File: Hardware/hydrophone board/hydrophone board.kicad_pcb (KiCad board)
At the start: 4 copper layers, 147.3 x 66 mm, 164 parts, among them J1 AudioJack3_Ground, J111 Conn_01x02, J121 Conn_01x02, J131 Conn_01x02, J141 Conn_01x02, J2 AudioJack3_Ground, J211 Conn_01x02, J221 Conn_01x02, J231 Conn_01x02, J241 Conn_01x02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

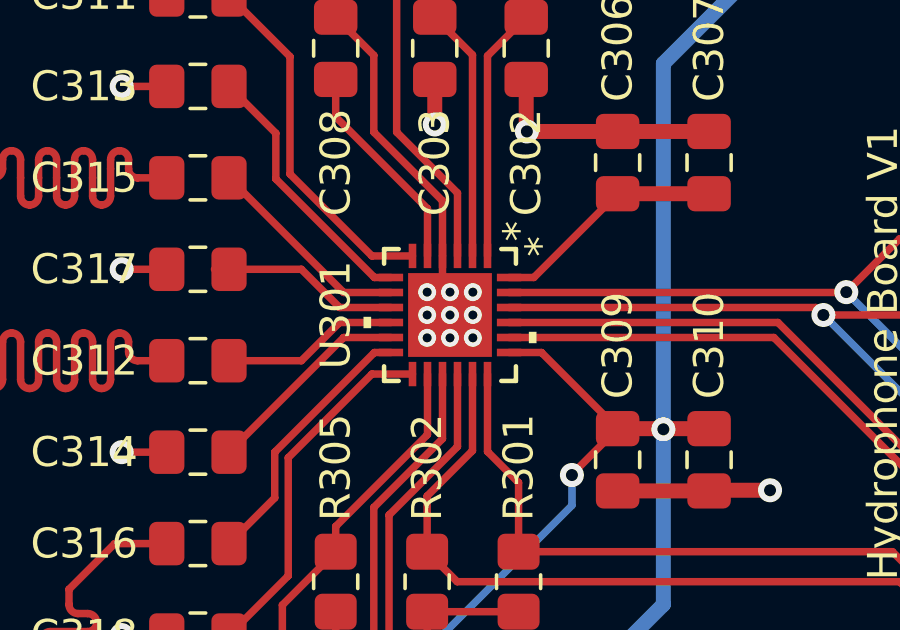
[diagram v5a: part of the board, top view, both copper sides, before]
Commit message: changed iovdd cap, thermal pad via size
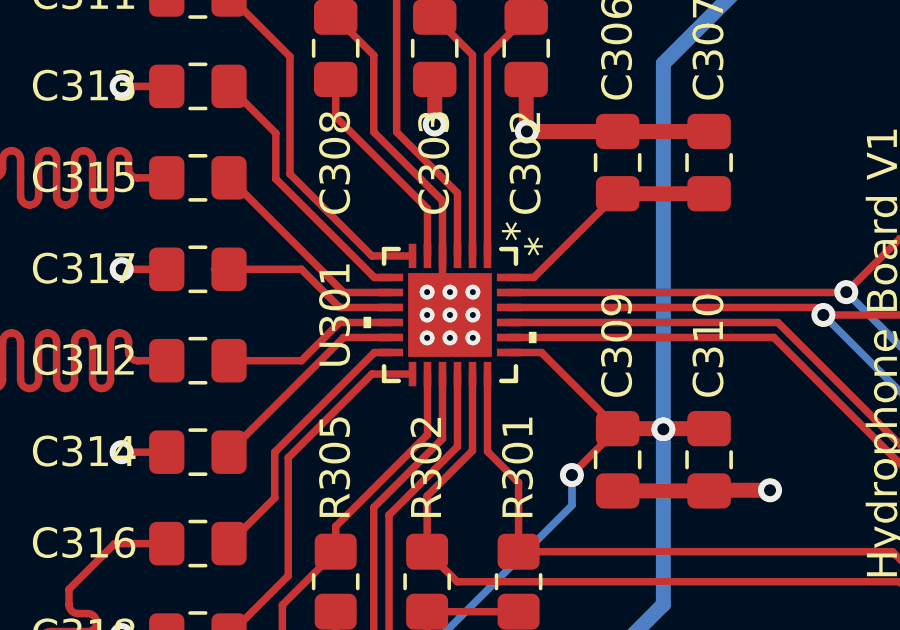
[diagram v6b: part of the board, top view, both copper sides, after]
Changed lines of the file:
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@@
   (segment (start 156.929 67.056) (end 155.4265 67.056) (width 0.25) (layer "F.Cu") (net 1))
   (via (at 146.05 77.724) (size 0.8) (drill 0.4) (layers "F.Cu" "B.Cu") (net 1))
-  (via (at 167.132 69.342) (size 0.6) (drill 0.3) (layers "F.Cu" "B.Cu") (net 1))
+  (via (at 167.132 69.342) (size 0.5) (drill 0.2) (layers "F.Cu" "B.Cu") (net 1))
   (via (at 177.038 87.884) (size 0.8) (drill 0.4) (layers "F.Cu" "B.Cu") (net 1))
   (via (at 135.128 45.72) (size 0.8) (drill 0.4) (layers "F.Cu" "B.Cu") (net 1))
   (via (at 172.974 95.25) (size 0.8) (drill 0.4) (layers "F.Cu" "B.Cu") (net 1))
-  (via (at 166.37 69.342) (size 0.6) (drill 0.3) (layers "F.Cu" "B.Cu") (net 1))
+  (via (at 166.37 69.342) (size 0.5) (drill 0.2) (layers "F.Cu" "B.Cu") (net 1))
   (via (at 98.044 81.28) (size 0.8) (drill 0.4) (layers "F.Cu" "B.Cu") (net 1))
   (via (at 101.6 73.66) (size 0.8) (drill 0.4) (layers "F.Cu" "B.Cu") (net 1))
@@
   (via (at 101.6 58.42) (size 0.8) (drill 0.4) (layers "F.Cu" "B.Cu") (net 1))
   (via (at 105.156 96.52) (size 0.8) (drill 0.4) (layers "F.Cu" "B.Cu") (net 1))
-  (via (at 167.132 68.58) (size 0.6) (drill 0.3) (layers "F.Cu" "B.Cu") (net 1))
+  (via (at 167.132 68.58) (size 0.5) (drill 0.2) (layers "F.Cu" "B.Cu") (net 1))
   (via (at 168.9315 62.4625) (size 0.8) (drill 0.4) (layers "F.Cu" "B.Cu") (net 1))
   (via (at 146.05 62.484) (size 0.8) (drill 0.4) (layers "F.Cu" "B.Cu") (net 1))
@@
   (via (at 71.374 97.563) (size 0.8) (drill 0.4) (layers "F.Cu" "B.Cu") (net 1))
   (via (at 165.1 97.282) (size 0.8) (drill 0.4) (layers "F.Cu" "B.Cu") (net 1))
-  (via (at 165.608 69.342) (size 0.6) (drill 0.3) (layers "F.Cu" "B.Cu") (net 1))
+  (via (at 165.608 69.342) (size 0.5) (drill 0.2) (layers "F.Cu" "B.Cu") (net 1))
   (via (at 120.904 86.3815) (size 0.8) (drill 0.4) (layers "F.Cu" "B.Cu") (net 1))
   (via (at 101.6 43.18) (size 0.8) (drill 0.4) (layers "F.Cu" "B.Cu") (net 1))
@@
   (via (at 117.348 76.2) (size 0.8) (drill 0.4) (layers "F.Cu" "B.Cu") (net 1))
   (via (at 164.084 83.804) (size 0.8) (drill 0.4) (layers "F.Cu" "B.Cu") (net 1))
-  (via (at 166.37 67.818) (size 0.6) (drill 0.3) (layers "F.Cu" "B.Cu") (net 1))
-  (via (at 167.132 67.818) (size 0.6) (drill 0.3) (layers "F.Cu" "B.Cu") (net 1))
+  (via (at 166.37 67.818) (size 0.5) (drill 0.2) (layers "F.Cu" "B.Cu") (net 1))
+  (via (at 167.132 67.818) (size 0.5) (drill 0.2) (layers "F.Cu" "B.Cu") (net 1))
   (via (at 177.038 74.422) (size 0.8) (drill 0.4) (layers "F.Cu" "B.Cu") (net 1))
-  (via (at 165.608 67.818) (size 0.6) (drill 0.3) (layers "F.Cu" "B.Cu") (net 1))
+  (via (at 165.608 67.818) (size 0.5) (drill 0.2) (layers "F.Cu" "B.Cu") (net 1))
   (via (at 175.768 97.282) (size 0.8) (drill 0.4) (layers "F.Cu" "B.Cu") (net 1))
   (via (at 172.974 93.98) (size 0.8) (drill 0.4) (layers "F.Cu" "B.Cu") (net 1))
@@
   (via (at 98.044 50.8) (size 0.8) (drill 0.4) (layers "F.Cu" "B.Cu") (net 1))
   (via (at 168.656 97.282) (size 0.8) (drill 0.4) (layers "F.Cu" "B.Cu") (net 1))
-  (via (at 165.608 68.58) (size 0.6) (drill 0.3) (layers "F.Cu" "B.Cu") (net 1))
+  (via (at 165.608 68.58) (size 0.5) (drill 0.2) (layers "F.Cu" "B.Cu") (net 1))
   (via (at 155.4265 79.248) (size 0.8) (drill 0.4) (layers "F.Cu" "B.Cu") (net 1))
   (via (at 105.156 50.8) (size 0.8) (drill 0.4) (layers "F.Cu" "B.Cu") (net 1))
   (via (at 146.05 47.244) (size 0.8) (drill 0.4) (layers "F.Cu" "B.Cu") (net 1))
   (via (at 105.156 81.2585) (size 0.8) (drill 0.4) (layers "F.Cu" "B.Cu") (net 1))
-  (via (at 166.37 68.58) (size 0.6) (drill 0.3) (layers "F.Cu" "B.Cu") (net 1))
+  (via (at 166.37 68.58) (size 0.5) (drill 0.2) (layers "F.Cu" "B.Cu") (net 1))
   (via (at 160.782 55.626) (size 0.8) (drill 0.4) (layers "F.Cu" "B.Cu") (net 1))
   (via (at 170.18 97.282) (size 0.8) (drill 0.4) (layers "F.Cu" "B.Cu") (net 1))

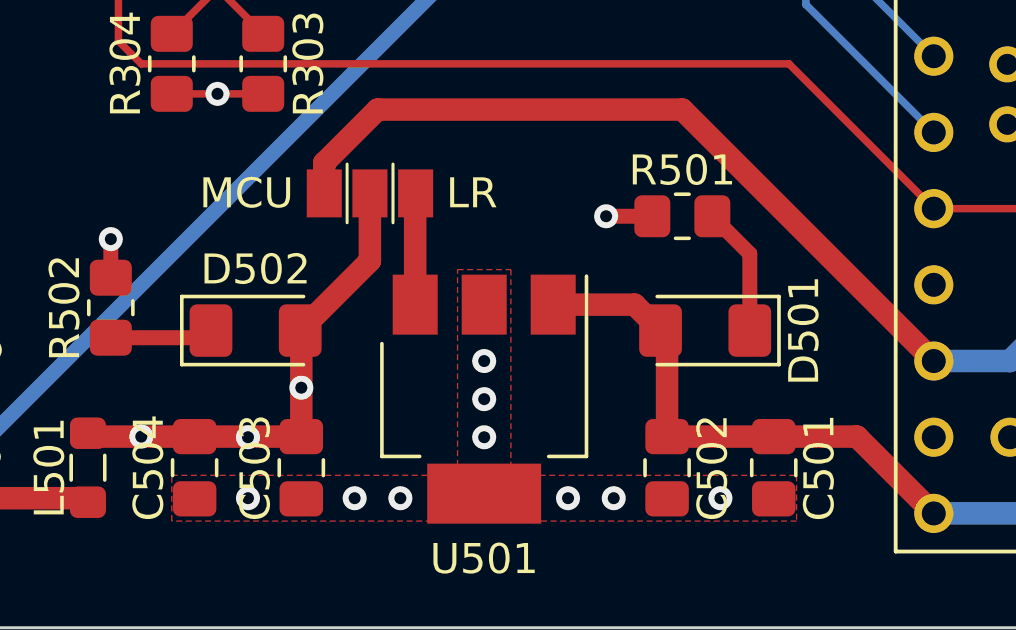
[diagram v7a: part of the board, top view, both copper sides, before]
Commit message: changed led footprint to 0805
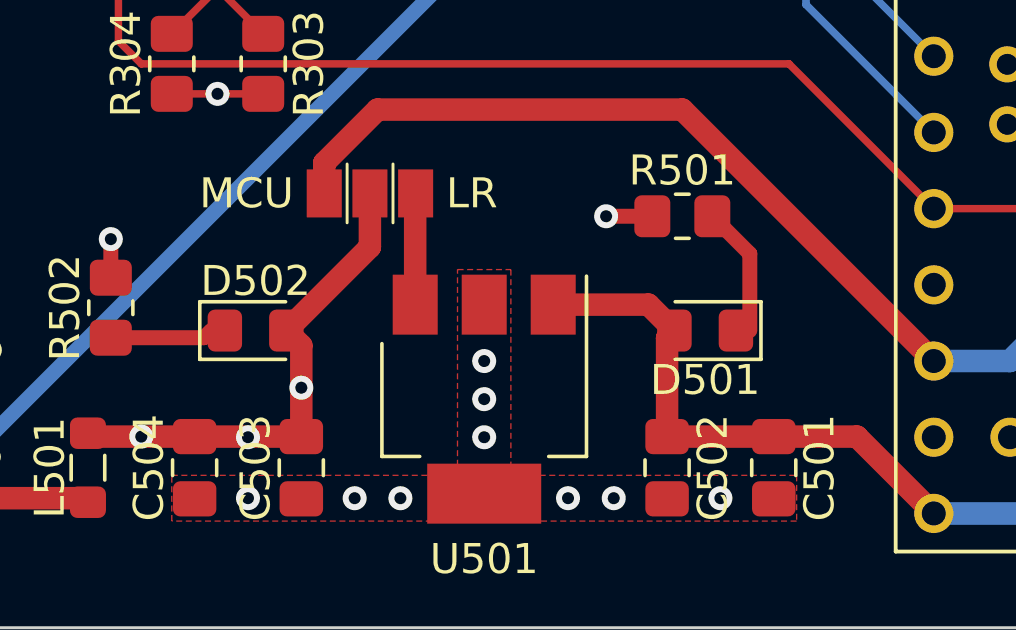
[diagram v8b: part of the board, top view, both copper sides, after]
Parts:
- C310: value 1u -> 10u
- D501, D502: footprint LED_SMD:LED_1206_3216Metric_Pad1.42x1.75mm_HandSolder -> LED_SMD:LED_0805_2012Metric_Pad1.15x1.40mm_HandSolder
- L501: value L_Ferrite_Small -> 600R @ 100MHz
- R301, R302: value 2k -> 2.2k
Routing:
- net +5V: track 42.8 -> 43.3 mm
